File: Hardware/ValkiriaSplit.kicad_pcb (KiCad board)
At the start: 2 copper layers, 284.5 x 111.4 mm, 320 parts, among them J1 BAT, J2 TagConnect, J3 0.96_TFT_MODULE, J4 BAT, J5 TagConnect, J6 0.96_TFT_MODULE, Q1 AO3401A, Q2 AO3401A, Q3 AO3401A, Q4 AO3401A, SW1 MSK12C02, SW10 PG1350, SW11 PG1350, SW12 PG1350, SW13 PG1350, SW14 PG1350, SW15 PG1350, SW16 PG1350, SW17 PG1350, SW18 PG1350, SW19 PG1350, SW2 SW_Push, SW20 PG1350, SW21 PG1350, SW22 PG1350, SW23 PG1350, SW24 PG1350, SW25 PG1350, SW26 PG1350, SW27 PG1350, SW28 PG1350, SW29 PG1350, SW3 MSK12C02, SW30 PG1350, SW31 PG1350, SW32 PG1350, SW33 PG1350, SW34 PG1350, SW35 PG1350, SW36 PG1350, SW37 ENCODER, SW38 PG1350, SW39 PG1350, SW4 MSK12C02, SW40 PG1350, SW41 PG1350, SW42 PG1350, SW43 PG1350, SW44 PG1350, SW45 PG1350, SW46 PG1350, SW47 PG1350, SW48 PG1350, SW49 PG1350, SW5 SW_Push, SW50 PG1350, SW51 PG1350, SW52 PG1350, SW53 PG1350, SW54 PG1350, SW55 PG1350, SW56 PG1350, SW57 PG1350, SW58 PG1350, SW59 PG1350, SW6 MSK12C02, SW60 PG1350, SW61 PG1350, SW62 PG1350, SW63 PG1350, SW64 PG1350, SW65 PG1350, SW66 PG1350, SW67 PG1350, SW68 ENCODER, SW7 PG1350, SW8 PG1350, SW9 PG1350, U1 XIAO-NRF52840-PLUS, U2 TPS61040DBV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

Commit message: MIP display and LED enable
Return of the LED enable via GPIO.
Changed the TFT display for a MPI panel. It's more expensive than an e-ink one, but the sharpness is really nice.
Need to remove the numbers row to go for a true Corne-ish layout.
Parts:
- removed the C43 at (113.0, 215.9)
- removed the C44 at (113.0, 218.4)
- removed the C75 at (259.0, 216.8)
- removed the C76 at (259.0, 219.3)
- removed the D120 at (258.8, 226.8)
- removed the D5 at (208.5, 234.0)
- removed the D6 at (313.2, 229.1)
- removed the D60 at (112.7, 225.9)
- removed Q3, Q4: AO3401A, Package_TO_SOT_SMD:SOT-23
- removed R21: 10K, Resistor_SMD:R_0603_1608Metric
- removed R22: 22, Resistor_SMD:R_0603_1608Metric
- removed R23, R24, R25, R26: 0, Resistor_SMD:R_0603_1608Metric
- removed the SW5 at (330.8, 229.5)
- removed the SW6 at (332.3, 225.0)
- removed the U2 at (180.0, 237.0)
- removed the U4 at (213.5, 237.0)
- added C13: 1n, Capacitor_SMD:C_0603_1608Metric, F.Cu at (254.0, 203.2)
- added C14: 1u, Capacitor_SMD:C_0603_1608Metric, F.Cu at (254.0, 205.7)
- added C45: 100n, Capacitor_SMD:C_0603_1608Metric, F.Cu at (112.3, 211.4)
- added C46: 100n, Capacitor_SMD:C_0603_1608Metric, F.Cu at (112.3, 213.9)
- added C77: 100n, Capacitor_SMD:C_0603_1608Metric, F.Cu at (280.3, 209.3)
- added C78: 100n, Capacitor_SMD:C_0603_1608Metric, F.Cu at (280.3, 211.8)
- added D118: 1N4148WT, Diode_SMD:D_SOD-523, F.Cu at (284.1, 209.3)
- added D58: 1N4148WT, Diode_SMD:D_SOD-523, F.Cu at (116.1, 211.3)
- added FB1: 600, Inductor_SMD:L_0603_1608Metric, F.Cu at (125.8, 209.8)
- added FB2: 600, Inductor_SMD:L_0603_1608Metric, F.Cu at (129.8, 197.2)
- added FB3: 600, Inductor_SMD:L_0603_1608Metric, F.Cu at (254.0, 208.2)
- added FB4: 600, Inductor_SMD:L_0603_1608Metric, F.Cu at (258.0, 195.7)
- added U1: TPS61040DBV, Package_TO_SOT_SMD:SOT-23-5, F.Cu at (126.4, 230.2)
- added U3: TPS61040DBV, Package_TO_SOT_SMD:SOT-23-5, F.Cu at (254.6, 228.6)
- C10: value 4.7u -> 10p; footprint Capacitor_SMD:C_1206_3216Metric -> Capacitor_SMD:C_0603_1608Metric
- C11: value 1u -> 4.7u; footprint Capacitor_SMD:C_0603_1608Metric -> Capacitor_SMD:C_1206_3216Metric
- C6: value 1u -> 1n
- C8: value 4.7u -> 1u; footprint Capacitor_SMD:C_1206_3216Metric -> Capacitor_SMD:C_0603_1608Metric
- C9: value 10p -> 4.7u; footprint Capacitor_SMD:C_0603_1608Metric -> Capacitor_SMD:C_1206_3216Metric
- J3, J6: value 0.96_TFT_MODULE -> 1.08_MIP_MODULE; footprint Custom_Parts:0.96_TFT_MODULE -> Custom_Parts:1.08_MIP_MODULE
- R1: value 100K -> 500
- R10: value 10K -> 100K
- R11: value 22 -> 10K
- R12: value 100K -> 470K
- R13: value 500 -> 150K
- R14: value 470K -> 0
- R15: value 150K -> 0
- R19, R8: value 100 -> 0
- R2: value 500 -> 100K
- R20: value 10K -> 0
- R3: value 470K -> 10K
- R4: value 150K -> 470K
- R5: value 0 -> 150K
- R9: value 10K -> 500
- SW4: value MSK12C02 -> SW_Push; footprint Custom_Parts:MSK12C02 -> Button_Switch_SMD:SW_SPST_TS-1088-xR020
- moved SW3 187.6 mm to (257.1, 224.0)
- moved D3 179.7 mm to (266.8, 196.1)
- moved R17 176.3 mm to (112.3, 216.4)
- moved R18 176.3 mm to (112.3, 218.9)
- moved R10 175.2 mm to (258.0, 200.7)
- moved R11 175.2 mm to (258.0, 203.2)
- moved R9 175.2 mm to (258.0, 198.2)
- moved Q2 163.7 mm to (259.6, 228.4)
- moved C7 109.0 mm to (125.8, 207.3)
- moved C1 81.6 mm to (125.8, 197.2)
- moved R1 77.8 mm to (129.8, 199.7)
- moved SW2 76.7 mm to (139.4, 204.9)
- moved R14 68.9 mm to (262.1, 195.7)
- moved D1 66.0 mm to (138.6, 197.6)
- moved R15 65.2 mm to (262.1, 198.2)
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- renumbered C13 to C15, C14 to C16, C15 to C17, C16 to C18, C17 to C19, C18 to C20, C19 to C21, C20 to C22, C21 to C23, C22 to C24, C23 to C25, C24 to C26, C25 to C27, C26 to C28, C27 to C29, C28 to C30, C29 to C31, C30 to C32, C31 to C33, C32 to C34, C33 to C35, C34 to C36, C35 to C37, C36 to C38, C37 to C39, C38 to C40, C39 to C41, C40 to C42, C41 to C43, C42 to C44, C45 to C47, C46 to C48, C47 to C49, C48 to C50, C49 to C51, C50 to C52, C51 to C53, C52 to C54, C53 to C55, C54 to C56, C55 to C57, C56 to C58, C57 to C59, C58 to C60, C59 to C61, C60 to C62, C61 to C63, C62 to C64, C63 to C65, C64 to C66, C65 to C67, C66 to C68, C67 to C69, C68 to C70, C69 to C71, C70 to C72, C71 to C73, C72 to C74, C73 to C75, C74 to C76, D12 to D10, D102 to D100, D103 to D101, D104 to D102, D105 to D103, D106 to D104, D107 to D105, D108 to D106, D109 to D107, D110 to D108, D111 to D109, D13 to D11, D112 to D110, D113 to D111, D114 to D112, D115 to D113, D116 to D114, D117 to D115, D118 to D116, D119 to D117, D121 to D119, D14 to D12, D122 to D120, D123 to D121, D124 to D122, D125 to D123, D126 to D124, D15 to D13, D16 to D14, D17 to D15, D18 to D16, D19 to D17, D20 to D18, D21 to D19, D22 to D20, D23 to D21, D24 to D22, D25 to D23, D26 to D24, D27 to D25, D28 to D26, D29 to D27, D30 to D28, D31 to D29, D32 to D30, D33 to D31, D34 to D32, D35 to D33, D36 to D34, D37 to D35, D38 to D36, D39 to D37, D40 to D38, D41 to D39, D42 to D40, D43 to D41, D44 to D42, D45 to D43, D46 to D44, D47 to D45, D48 to D46, D49 to D47, D50 to D48, D51 to D49, D7 to D5, D52 to D50, D53 to D51, D54 to D52, D55 to D53, D56 to D54, D57 to D55, D58 to D56, D59 to D57, D61 to D59, D8 to D6, D62 to D60, D63 to D61, D64 to D62, D65 to D63, D66 to D64, D67 to D65, D68 to D66, D69 to D67, D70 to D68, D71 to D69, D9 to D7, D72 to D70, D73 to D71, D74 to D72, D75 to D73, D76 to D74, D77 to D75, D78 to D76, D79 to D77, D80 to D78, D81 to D79, D10 to D8, D82 to D80, D83 to D81, D84 to D82, D85 to D83, D86 to D84, D87 to D85, D88 to D86, D89 to D87, D90 to D88, D91 to D89, D11 to D9, D92 to D90, D93 to D91, D94 to D92, D95 to D93, D96 to D94, D97 to D95, D98 to D96, D99 to D97, D100 to D98, D101 to D99, SW12 to SW10, SW13 to SW11, SW14 to SW12, SW15 to SW13, SW16 to SW14, SW17 to SW15, SW18 to SW16, SW19 to SW17, SW20 to SW18, SW21 to SW19, SW22 to SW20, SW23 to SW21, SW24 to SW22, SW25 to SW23, SW26 to SW24, SW27 to SW25, SW28 to SW26, SW29 to SW27, SW30 to SW28, SW31 to SW29, SW32 to SW30, SW33 to SW31, SW34 to SW32, SW35 to SW33, SW36 to SW34, SW37 to SW35, SW38 to SW36, SW39 to SW37, SW40 to SW38, SW41 to SW39, SW42 to SW40, SW43 to SW41, SW44 to SW42, SW45 to SW43, SW46 to SW44, SW47 to SW45, SW48 to SW46, SW49 to SW47, SW50 to SW48, SW51 to SW49, SW7 to SW5, SW52 to SW50, SW53 to SW51, SW54 to SW52, SW55 to SW53, SW56 to SW54, SW57 to SW55, SW58 to SW56, SW59 to SW57, SW60 to SW58, SW61 to SW59, SW8 to SW6, SW62 to SW60, SW63 to SW61, SW64 to SW62, SW65 to SW63, SW66 to SW64, SW67 to SW65, SW68 to SW66, SW9 to SW7, SW10 to SW8, SW11 to SW9, U1 to U2, U3 to U4
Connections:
- C10 pad 2: GND -> /Control_Right/VFB
- C11 pad 1: /Control_Right/LCD_RES -> 5VR
- C12 pad 1: 3V3R -> /Control_Right/MIP_VDDA
- C12 pad 2: GND -> /Control_Right/MIP_VSSA
- C5 pad 1: /Control_Left/LCD_RES -> /Control_Left/MIP_VDDA
- C5 pad 2: GND -> /Control_Left/MIP_VSSA
- C6 pad 1: 3V3L -> /Control_Left/MIP_EN
- C7 pad 1: VBUSR -> 3V3L
- C8 pad 1: VREGR -> VBUSR
- C9 pad 1: 5VR -> VREGR
- C9 pad 2: /Control_Right/VFB -> GND
- D1 pad 1: /Control_Left/VCOM -> VREGL
- D3 pad 1: 3V3L -> VREGR
- D3 pad 2: /Control_Left/LCD_RES -> VBUSR
- D4 pad 1: /Control_Right/VCOM -> 5VR
- D4 pad 2: VBUSR -> /Control_Right/VSW
- J3 pad 1: /Control_Left/BKL -> /Control_Left/MIP_SCK
- J3 pad 2: GND -> /Control_Left/MIP_MOSI
- J3 pad 3: /Control_Left/LCD_RES -> /Control_Left/MIP_CS
- J3 pad 4: /Control_Left/LCD_DC -> GND
- J3 pad 5: /Control_Left/LCD_MOSI -> /Control_Left/MIP_EN
- J3 pad 6: /Control_Left/LCD_SCK -> /Control_Left/MIP_VDDA
- J3 pad 8: /Control_Left/LCD_CS -> GND
- J6 pad 1: /Control_Right/BKL -> /Control_Right/MIP_SCK
- J6 pad 2: GND -> /Control_Right/MIP_MOSI
- J6 pad 3: /Control_Right/LCD_RES -> /Control_Right/MIP_CS
- J6 pad 4: /Control_Right/LCD_DC -> GND
- J6 pad 5: /Control_Right/LCD_MOSI -> /Control_Right/MIP_EN
- J6 pad 6: /Control_Right/LCD_SCK -> /Control_Right/MIP_VDDA
- J6 pad 8: /Control_Right/LCD_CS -> GND
- Q1 pad 2: /Control_Left/VCOM -> VREGL
- Q2 pad 1: /Control_Left/BKLG -> VBUSR
- Q2 pad 2: /Control_Left/BKLD -> VREGR
- Q2 pad 3: 3V3L -> VBATR
- R1 pad 1: VBUSL -> /Control_Left/LED_DATA
- R1 pad 2: GND -> LED_DATA_L
- R10 pad 1: /Control_Left/BKLD -> VBUSR
- R10 pad 2: /Control_Left/BKLG -> GND
- R11 pad 1: /Control_Left/BKLD -> GND
- R11 pad 2: /Control_Left/BKL -> /Control_Right/LED_EN
- R12 pad 1: VBUSR -> 5VR
- R12 pad 2: GND -> /Control_Right/VFB
- R13 pad 1: /Control_Right/LED_DATA -> /Control_Right/VFB
- R13 pad 2: LED_DATA_R -> GND
- R14 pad 1: 5VR -> Net-(U4-P1.15_MOSI)
- R14 pad 2: /Control_Right/VFB -> /Control_Right/MIP_MOSI
- R15 pad 1: /Control_Right/VFB -> Net-(U4-P1.14_MISO)
- R15 pad 2: GND -> /Control_Right/MIP_CS
- R16 pad 1: Net-(U3-P1.15_MOSI) -> Net-(U4-P1.13_SCK)
- R16 pad 2: /Control_Right/LCD_MOSI -> /Control_Right/MIP_SCK
- R17 pad 1: Net-(U3-P1.14_MISO) -> ENC_CW_L
- R17 pad 2: /Control_Right/LCD_DC -> /Matrix_Left/ENC_CW
- R18 pad 1: Net-(U3-P1.13_SCK) -> ENC_CC_L
- R18 pad 2: /Control_Right/LCD_SCK -> /Matrix_Left/ENC_CC
- R19 pad 1: /Control_Right/LCD_BKL -> ENC_CW_R
- R19 pad 2: /Control_Right/BKLG -> /Matrix_Right/ENC_CW
- R2 pad 1: /Control_Left/LED_DATA -> VBUSL
- R2 pad 2: LED_DATA_L -> GND
- R20 pad 1: 3V3R -> ENC_CC_R
- R20 pad 2: /Control_Right/LCD_RES -> /Matrix_Right/ENC_CC
- R3 pad 1: 5VL -> GND
- R3 pad 2: /Control_Left/VFB -> /Control_Left/LED_EN
- R4 pad 1: /Control_Left/VFB -> 5VL
- R4 pad 2: GND -> /Control_Left/VFB
- R5 pad 1: Net-(U1-P1.15_MOSI) -> /Control_Left/VFB
- R5 pad 2: /Control_Left/LCD_MOSI -> GND
- R6 pad 1: Net-(U1-P1.14_MISO) -> Net-(U2-P1.15_MOSI)
- R6 pad 2: /Control_Left/LCD_DC -> /Control_Left/MIP_MOSI
- R7 pad 1: Net-(U1-P1.13_SCK) -> Net-(U2-P1.14_MISO)
- R7 pad 2: /Control_Left/LCD_SCK -> /Control_Left/MIP_CS
- R8 pad 1: /Control_Left/LCD_BKL -> Net-(U2-P1.13_SCK)
- R8 pad 2: /Control_Left/BKLG -> /Control_Left/MIP_SCK
- R9 pad 1: 3V3L -> /Control_Right/LED_DATA
- R9 pad 2: /Control_Left/LCD_RES -> LED_DATA_R
- SW3 pad 2: /Control_Left/VCOM -> /Control_Right/VBAT
- SW3 pad 3: VREGL -> VBATR
- SW4 pad 1: unconnected-(SW4-A-Pad1) -> /Control_Right/~{RESET}
- SW4 pad 2: /Control_Right/VBAT -> GND
- U2 pad 10: Net-(U1-P1.14_MISO) -> Net-(U2-P1.14_MISO)
- U2 pad 11: Net-(U1-P1.15_MOSI) -> Net-(U2-P1.15_MOSI)
- U2 pad 22: /Control_Left/LCD_BKL -> /Control_Left/MIP_EN
- U2 pad 7: /Control_Left/LCD_CS -> /Control_Left/LED_EN
- U2 pad 9: Net-(U1-P1.13_SCK) -> Net-(U2-P1.13_SCK)
- U4 pad 10: Net-(U3-P1.14_MISO) -> Net-(U4-P1.14_MISO)
- U4 pad 11: Net-(U3-P1.15_MOSI) -> Net-(U4-P1.15_MOSI)
- U4 pad 22: /Control_Right/LCD_BKL -> /Control_Right/MIP_EN
- U4 pad 7: /Control_Right/LCD_CS -> /Control_Right/LED_EN
- U4 pad 9: Net-(U3-P1.13_SCK) -> Net-(U4-P1.13_SCK)
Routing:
- removed copper zone on F.Cu, net /Control_Left/VFB
- removed copper zone on F.Cu, net /Control_Left/VSW
- removed copper zone on F.Cu, net /Control_Right/VFB
- removed copper zone on F.Cu, net /Control_Right/VSW
- removed copper zone on F.Cu, net VREGL
- removed copper zone on F.Cu, net VREGR

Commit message: Row removal and key layout
Removed the number row.
Adjusted the spacebar position and changed it to 1u.
Need to consider what to do for one of the halfs if its screen is to be removed.
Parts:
- removed the C16 at (160.6, 72.0)
- removed the C19 at (141.5, 69.6)
- removed the C23 at (122.5, 67.2)
- removed the C27 at (103.4, 69.6)
- removed the C31 at (84.4, 74.4)
- removed the C35 at (65.3, 74.4)
- removed the C48 at (242.9, 77.3)
- removed the C51 at (262.0, 75.0)
- removed the C55 at (281.0, 72.5)
- removed the C59 at (300.1, 75.0)
- removed the C63 at (319.1, 79.8)
- removed C67: 1u, Capacitor_SMD:C_0603_1608Metric
- removed D105, D114: 1N4148WT, Diode_SMD:D_SOD-523
- removed the D11 at (154.3, 79.9)
- removed D110: SK6812MINI-E, Custom_Parts:LED_SK6812MINI-E_3.2x2.8mm_P1.5mm_ReverseMount
- removed the D18 at (124.4, 70.2)
- removed the D20 at (135.2, 77.5)
- removed the D27 at (105.4, 72.6)
- removed the D29 at (116.2, 75.1)
- removed the D36 at (86.3, 77.4)
- removed the D38 at (97.1, 77.5)
- removed the D45 at (78.1, 82.3)
- removed the D50 at (67.3, 77.4)
- removed the D54 at (59.0, 82.3)
- removed the D6 at (162.5, 75.0)
- removed the D66 at (237.5, 75.0)
- removed the D69 at (256.5, 72.6)
- removed the D71 at (229.2, 79.9)
- removed the D78 at (275.6, 70.2)
- removed the D80 at (248.2, 77.5)
- removed the D87 at (294.6, 72.6)
- removed the D89 at (267.3, 75.1)
- removed the D9 at (143.5, 72.6)
- removed the D96 at (313.7, 77.4)
- removed the D98 at (286.3, 77.5)
- removed the SW10 at (140.9, 82.6)
- removed the SW15 at (121.9, 80.2)
- removed the SW20 at (102.8, 82.6)
- removed the SW25 at (83.8, 87.4)
- removed the SW30 at (64.8, 87.4)
- removed the SW36 at (234.9, 85.0)
- removed the SW41 at (254.0, 82.6)
- removed the SW46 at (273.0, 80.2)
- removed the SW5 at (160.0, 85.0)
- removed the SW51 at (292.1, 82.6)
- removed SW56, SW61: PG1350, Custom_Parts:PG1350_1.00u_PCB
- moved J6 103.4 mm to (216.5, 220.6)
- moved SW54 80.8 mm to (238.7, 211.7)
- moved D62 15.4 mm to (217.7, 168.1), turned to -66 degrees
- moved SW33 12.6 mm to (225.0, 170.4), turned to -156 degrees
- moved SW8 10.6 mm to (170.3, 168.4), turned to 156 degrees
- moved D14 8.99 mm to (167.1, 161.4), turned to -114 degrees
- moved J2 8.60 mm to (183.6, 85.0)
- moved J5 8.60 mm to (216.4, 85.0)
- moved C23 7.86 mm to (176.1, 156.7), turned to -24 degrees
- moved U2 6.00 mm to (183.6, 75.0)
- moved U4 6.00 mm to (216.4, 75.0)
- moved SW29 5.47 mm to (183.6, 139.5)
- moved D65 4.93 mm to (223.3, 160.3), turned to 24 degrees
- moved D17 4.93 mm to (176.7, 160.3), turned to 156 degrees
- moved C49 4.36 mm to (229.2, 160.2), turned to 24 degrees
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- renumbered C44 to C15, C41 to C16, C42 to C17, C40 to C18, C37 to C19, C38 to C20, C36 to C21, C33 to C22, C34 to C23, C32 to C24, C29 to C25, C30 to C26, C28 to C27, C25 to C28, C26 to C29, C24 to C30, C21 to C31, C22 to C32, C20 to C33, C17 to C34, C18 to C35, C43 to C36, C39 to C37, C15 to C38, C45 to C39, C46 to C40, C76 to C41, C73 to C42, C74 to C43, C72 to C44, C69 to C45, C70 to C46, C68 to C47, C65 to C48, C66 to C49, C64 to C50, C61 to C51, C62 to C52, C60 to C53, C57 to C54, C58 to C55, C53 to C57, C54 to C58, C52 to C59, C49 to C60, C50 to C61, C75 to C62, C71 to C63, C47 to C64, C77 to C65, C78 to C66, D53 to D10, D65 to D100, D12 to D11, D13 to D12, D14 to D13, D15 to D14, D51 to D15, D43 to D16, D44 to D17, D21 to D18, D22 to D19, D23 to D20, D24 to D21, D37 to D22, D34 to D23, D35 to D24, D30 to D25, D31 to D26, D32 to D27, D33 to D28, D28 to D29, D39 to D30, D40 to D31, D41 to D32, D42 to D33, D25 to D34, D26 to D35, D19 to D36, D46 to D37, D47 to D38, D48 to D39, D49 to D40, D16 to D41, D17 to D42, D10 to D43, D55 to D44, D56 to D45, D57 to D46, D58 to D47, D7 to D48, D8 to D49, D64 to D5, D63 to D50, D59 to D51, D5 to D52, D124 to D53, D121 to D54, D122 to D55, D120 to D56, D112 to D57, D113 to D58, D72 to D59, D61 to D6, D73 to D60, D74 to D61, D75 to D62, D111 to D63, D103 to D64, D104 to D65, D81 to D66, D82 to D67, D83 to D68, D84 to D69, D62 to D7, D97 to D70, D94 to D71, D95 to D72, D90 to D73, D91 to D74, D92 to D75, D93 to D76, D88 to D77, D99 to D78, D100 to D79, D60 to D8, D101 to D80, D102 to D81, D85 to D82, D86 to D83, D79 to D84, D106 to D85, D107 to D86, D108 to D87, D109 to D88, D76 to D89, D52 to D9, D77 to D90, D70 to D91, D115 to D92, D116 to D93, D117 to D94, D118 to D95, D67 to D96, D68 to D97, D123 to D98, D119 to D99, SW12 to SW10, SW13 to SW11, SW14 to SW12, SW16 to SW13, SW17 to SW14, SW18 to SW15, SW19 to SW16, SW21 to SW17, SW22 to SW18, SW23 to SW19, SW24 to SW20, SW26 to SW21, SW27 to SW22, SW28 to SW23, SW29 to SW24, SW31 to SW25, SW32 to SW26, SW33 to SW27, SW34 to SW28, SW35 to SW29, SW37 to SW30, SW38 to SW31, SW39 to SW32, SW40 to SW33, SW42 to SW34, SW43 to SW35, SW44 to SW36, SW45 to SW37, SW47 to SW38, SW48 to SW39, SW49 to SW40, SW50 to SW41, SW52 to SW42, SW53 to SW43, SW54 to SW44, SW55 to SW45, SW57 to SW46, SW58 to SW47, SW59 to SW48, SW60 to SW49, SW6 to SW5, SW62 to SW50, SW63 to SW51, SW64 to SW52, SW65 to SW53, SW66 to SW54, SW7 to SW6, SW8 to SW7, SW9 to SW8, SW11 to SW9
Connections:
- D11 pad 1: ROW2_L -> ROW1_L
- D12 pad 1: ROW3_L -> ROW2_L
- D13 pad 1: ROW4_L -> ROW3_L
- D14 pad 1: ROW5_L -> ROW4_L
- D18 pad 1: ROW2_L -> ROW1_L
- D19 pad 1: ROW3_L -> ROW2_L
- D20 pad 1: ROW4_L -> ROW3_L
- D21 pad 1: ROW5_L -> ROW4_L
- D25 pad 1: ROW2_L -> ROW1_L
- D26 pad 1: ROW3_L -> ROW2_L
- D27 pad 1: ROW4_L -> ROW3_L
- D28 pad 1: ROW5_L -> ROW4_L
- D30 pad 1: ROW2_L -> ROW1_L
- D31 pad 1: ROW3_L -> ROW2_L
- D32 pad 1: ROW4_L -> ROW3_L
- D33 pad 1: ROW5_L -> ROW4_L
- D37 pad 1: ROW2_L -> ROW1_L
- D38 pad 1: ROW3_L -> ROW2_L
- D39 pad 1: ROW4_L -> ROW3_L
- D40 pad 1: ROW5_L -> ROW4_L
- D43 pad 2: Net-(D10-DIN) (its old number) -> Net-(D43-DIN)
- D44 pad 1: ROW2_L -> ROW1_L
- D45 pad 1: ROW3_L -> ROW2_L
- D46 pad 1: ROW4_L -> ROW3_L
- D47 pad 1: ROW5_L -> ROW4_L
- D48 pad 4: Net-(D10-DIN) (its old number) -> Net-(D48-DOUT)
- D50 pad 4: Net-(D61-DIN) -> Net-(D43-DIN)
- D51 pad 2: Net-(D50-DOUT) -> Net-(D48-DOUT)
- D54 pad 2: Net-(D121-DIN) -> LED_DATA_R
- D59 pad 1: ROW2_R -> ROW1_R
- D6 pad 2: Net-(D61-DIN) -> LED_DATA_L
- D60 pad 1: ROW3_R -> ROW2_R
- D61 pad 1: ROW4_R -> ROW3_R
- D62 pad 1: ROW5_R -> ROW4_R
- D66 pad 1: ROW2_R -> ROW1_R
- D67 pad 1: ROW3_R -> ROW2_R
- D68 pad 1: ROW4_R -> ROW3_R
- D69 pad 1: ROW5_R -> ROW4_R
- D73 pad 1: ROW2_R -> ROW1_R
- D74 pad 1: ROW3_R -> ROW2_R
- D75 pad 1: ROW4_R -> ROW3_R
- D76 pad 1: ROW5_R -> ROW4_R
- D78 pad 1: ROW2_R -> ROW1_R
- D79 pad 1: ROW3_R -> ROW2_R
- D80 pad 1: ROW4_R -> ROW3_R
- D81 pad 1: ROW5_R -> ROW4_R
- D85 pad 1: ROW2_R -> ROW1_R
- D86 pad 1: ROW3_R -> ROW2_R
- D87 pad 1: ROW4_R -> ROW3_R
- D88 pad 1: ROW5_R -> ROW4_R
- D91 pad 2: Net-(D67-DOUT) -> Net-(D91-DIN)
- D92 pad 1: ROW2_R -> ROW1_R
- D93 pad 1: ROW3_R -> ROW2_R
- D94 pad 1: ROW4_R -> ROW3_R
- D95 pad 1: ROW5_R -> ROW4_R
- D96 pad 4: Net-(D67-DOUT) -> Net-(D96-DOUT)
- D98 pad 4: Net-(D121-DIN) -> Net-(D91-DIN)
- D99 pad 2: Net-(D110-DOUT) -> Net-(D96-DOUT)
- U2 pad 6: ROW5_L -> unconnected-(U2-P0.05_SCL-Pad6)
- U4 pad 6: ROW5_R -> unconnected-(U4-P0.05_SCL-Pad6)
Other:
- board size 284.5 x 111.4 mm -> 284.5 x 92.4 mm

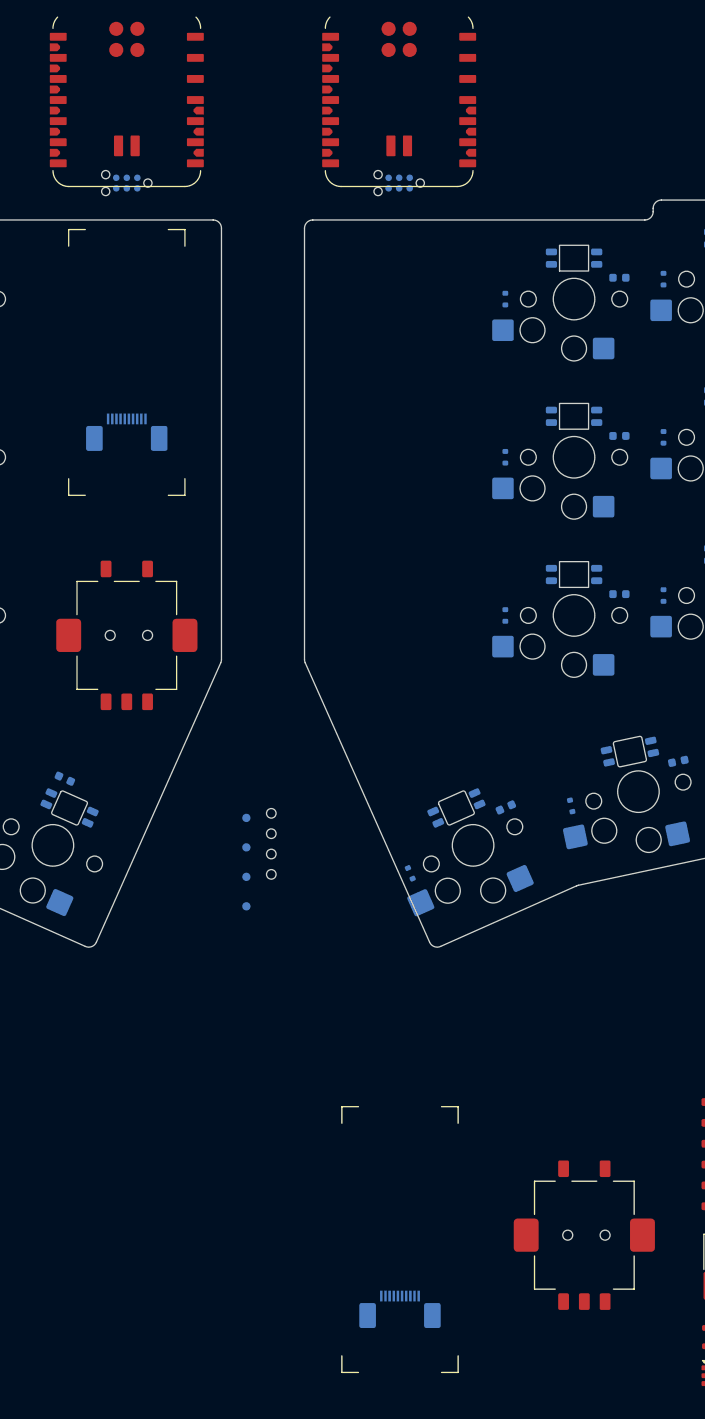
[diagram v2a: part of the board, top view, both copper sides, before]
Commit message: Debug connector
Updated the debug connector for a custom one.
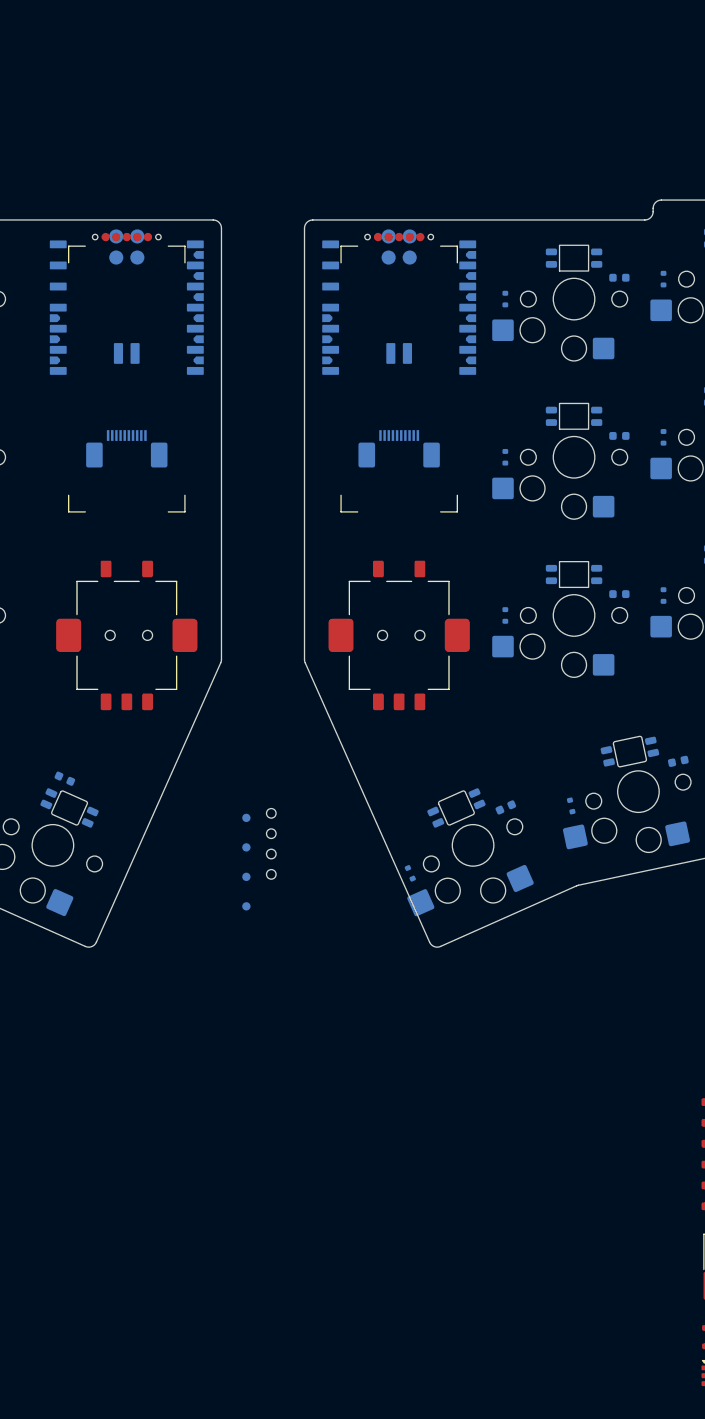
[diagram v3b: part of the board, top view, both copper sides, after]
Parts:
- C15, C16, C17, C18, C19, C20, C21, C22, C23, C24, C25, C26, C27, C28, C29, C30, C31, C32, C33, C34, C35, C36, C37, C38, C41, C42, C43, C44, C45, C46, C47, C48, C49, C50, C51, C52, C53, C54, C55, C56, C57, C58, C59, C60, C61, C62, C63, C64: value 1u -> 100n
- J2, J5: value TagConnect -> JTAG; footprint Connector:Tag-Connect_TC2030-IDC-NL_2x03_P1.27mm_Vertical -> Custom_Parts:JTAG_SWD_1X05_1.27MM_COMBO; moved to F.Cu
- U2, U4: moved to B.Cu
- moved J6 103.6 mm to (216.4, 117.0)
- moved SW54 75.6 mm to (216.4, 139.5)
- moved U2 25.0 mm to (183.6, 100.0)
- moved U4 25.0 mm to (216.4, 100.0)
- moved J2 7.53 mm to (179.8, 91.5), turned to 0 degrees
- moved J5 7.53 mm to (220.2, 91.5)
- moved J3 2.00 mm to (183.6, 117.0)

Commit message: Board outline and routing
Enlarged the board outline by 0.5mm for proper fitment of the switch receptacles.
Updated the footprint for the switch receptacles.
Changed the JTAG connector for a custom one.
Need to review the size of the PCB area dedicated to the MCU and the screen.
Need to consider removing the additional reset button.
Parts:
- C1, C10, C11, C12, C13, C14, C2, C3, C39, C4, C40, C5, C6, C65, C66, C7, C8, C9, D47, D95, FB1, FB2, FB3, FB4, J1, J4, L1, L2, Q1, Q2, R1, R10, R11, R12, R13, R14, R15, R16, R17, R18, R19, R2, R20, R3, R4, R5, R6, R7, R8, R9, SW1, SW2, SW3, SW4, U1, U3: moved to B.Cu
- D1, D2, D3, D4: value DSK24 -> DSL14; moved to B.Cu
- H1, H2, H3, H4: value MountingHole -> Tooling
- SW10, SW11, SW12, SW13, SW14, SW15, SW16, SW17, SW18, SW19, SW20, SW21, SW22, SW23, SW24, SW25, SW26, SW27, SW28, SW30, SW31, SW32, SW33, SW34, SW35, SW36, SW37, SW38, SW39, SW40, SW41, SW42, SW43, SW44, SW45, SW46, SW47, SW48, SW49, SW5, SW50, SW51, SW52, SW53, SW6, SW7, SW8, SW9: footprint Custom_Parts:PG1350_1.00u_PCB -> Custom_Parts:PG1350_1.00u_PCB_TIGHT
- moved SW4 130.4 mm to (216.4, 83.4), turned to 180 degrees
- moved SW2 129.3 mm to (183.6, 83.4), turned to 180 degrees
- moved R1 115.0 mm to (171.0, 92.4), turned to 180 degrees
- moved FB1 113.8 mm to (184.8, 112.4), turned to 90 degrees
- moved SW1 113.6 mm to (193.4, 132.0), turned to -90 degrees
- moved C7 112.8 mm to (186.8, 112.4), turned to 90 degrees
- moved R9 109.7 mm to (229.0, 92.4)
- moved C5 106.4 mm to (182.8, 112.4), turned to -90 degrees
- moved SW3 104.9 mm to (206.6, 132.0), turned to 90 degrees
- moved FB3 102.7 mm to (217.2, 112.4), turned to 90 degrees
- moved C14 99.6 mm to (219.2, 112.4), turned to 90 degrees
- moved FB2 99.0 mm to (180.8, 112.4), turned to -90 degrees
- moved C6 98.7 mm to (180.8, 122.8), turned to -90 degrees
- moved C12 96.5 mm to (215.2, 112.4), turned to -90 degrees
- moved R8 95.5 mm to (186.8, 122.8), turned to 90 degrees
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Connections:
- J2 pad 2: /Control_Left/SWDIO -> /Control_Left/SWDCLK
- J2 pad 3: /Control_Left/~{RESET} -> /Control_Left/SWDIO
- J2 pad 4: /Control_Left/SWDCLK -> /Control_Left/~{RESET}
- J5 pad 2: /Control_Right/SWDIO -> /Control_Right/SWDCLK
- J5 pad 3: /Control_Right/~{RESET} -> /Control_Right/SWDIO
- J5 pad 4: /Control_Right/SWDCLK -> /Control_Right/~{RESET}
- SW1 pad 1: unconnected-(SW1-A-Pad1) -> VBATL
- SW1 pad 3: VBATL -> unconnected-(SW1-C-Pad3)
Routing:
- net /Control_Left/MIP_VDDA: track 0.00 -> 9.06 mm, vias 0 -> 2
- net /Control_Right/MIP_VDDA: track 0.00 -> 9.06 mm, vias 0 -> 2
- net /Control_Right/MIP_EN: track 0.00 -> 7.97 mm
- net /Control_Left/MIP_EN: track 0.00 -> 7.97 mm
- net /Control_Right/MIP_CS: track 0.00 -> 7.51 mm
- net /Control_Left/MIP_CS: track 0.00 -> 7.51 mm
- net /Control_Right/MIP_SCK: track 0.00 -> 6.89 mm
- net /Control_Right/MIP_MOSI: track 0.00 -> 6.89 mm
- net /Control_Left/MIP_SCK: track 0.00 -> 6.89 mm
- net /Control_Left/MIP_MOSI: track 0.00 -> 6.89 mm
- net 3V3L: track 0.00 -> 5.23 mm
- net 3V3R: track 0.00 -> 5.23 mm
- net /Control_Right/MIP_VSSA: track 0.00 -> 4.53 mm
- net /Control_Left/MIP_VSSA: track 0.00 -> 4.53 mm
- net /Control_Right/SWDCLK: track 0.00 -> 4.16 mm, vias 0 -> 1
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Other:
- board size 284.5 x 92.4 mm -> 285.5 x 93.5 mm

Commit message: Layout and routing
Updated the position of some RGB LEDs.
Routed the left side columns.
This is a temporary commit in order to test different LED routing.
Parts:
- moved D10 95.3 mm to (67.3, 134.5)
- moved D22 95.3 mm to (162.5, 132.1)
- moved D29 95.3 mm to (162.5, 113.1)
- moved D34 78.0 mm to (86.3, 96.4)
- moved D41 77.5 mm to (67.3, 96.4)
- moved D48 57.6 mm to (67.3, 115.5)
- moved D15 57.4 mm to (143.5, 129.7)
- moved D36 57.4 mm to (143.5, 110.7)
- moved D7 57.4 mm to (86.3, 134.5)
- moved J4 41.0 mm to (240.0, 200.0)
- moved J1 40.9 mm to (160.0, 200.0)
- moved Q1 36.2 mm to (180.6, 208.7)
- moved C1 36.2 mm to (169.9, 196.4)
- moved R3 36.2 mm to (169.9, 204.0)
- moved U1 36.2 mm to (180.7, 204.3)
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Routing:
- net COL1_L: track 0.00 -> 76.0 mm
- net COL3_L: track 0.00 -> 72.7 mm
- net COL2_L: track 0.00 -> 72.4 mm
- net COL6_L: track 0.00 -> 65.3 mm
- net COL5_L: track 0.00 -> 65.3 mm
- net COL4_L: track 0.00 -> 65.3 mm
- net 5VL: track 0.00 -> 49.3 mm
- net Net-(U2-P1.15_MOSI): track 0.00 -> 40.7 mm
- net Net-(U2-P1.14_MISO): track 0.00 -> 32.9 mm
- net Net-(U2-P1.13_SCK): track 0.00 -> 30.3 mm, vias 0 -> 2
- net VBATL: track 0.00 -> 27.4 mm
- net /Control_Left/MIP_EN: track 7.97 -> 34.7 mm
- net VBUSL: track 0.00 -> 23.5 mm
- net /Control_Left/LED_DATA: track 0.00 -> 23.0 mm
- net 3V3L: track 5.23 -> 26.0 mm
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- added copper zone on B.Cu, net GND
- added copper zone on F.Cu, net GND
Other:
- outline, holes or cut-outs redrawn

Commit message: Display model and layout
Updated the 3D model and footprint for the MIP display. It now sits further from the PCB.
Continued the layout and routing of the left side PCB.
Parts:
- C11, C2, C4, C9: value 4.7u -> 10u; footprint Capacitor_SMD:C_1206_3216Metric -> Capacitor_SMD:C_0603_1608Metric
- J3, J6: footprint Custom_Parts:1.08_MIP_MODULE -> Custom_Parts:1.08_MIP_MODULE_TALL
- moved D23 99.0 mm to (176.7, 160.3), turned to 156 degrees
- moved D17 94.0 mm to (86.3, 134.5), turned to 180 degrees
- moved D34 89.9 mm to (155.8, 153.5), turned to 168 degrees
- moved D41 83.2 mm to (143.5, 129.7)
- moved D48 76.4 mm to (143.5, 110.7)
- moved D24 69.5 mm to (86.3, 153.6), turned to 180 degrees
- moved D35 66.7 mm to (67.3, 153.6)
- moved D51 61.9 mm to (143.5, 91.6)
- moved D22 59.5 mm to (105.4, 148.8)
- moved D16 57.4 mm to (162.5, 132.1)
- moved D52 57.2 mm to (67.3, 96.4)
- moved D29 47.6 mm to (134.0, 151.2)
- moved D49 42.6 mm to (67.3, 115.5)
- moved D42 40.7 mm to (67.3, 134.5)
- moved D15 38.1 mm to (105.4, 129.7)
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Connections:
- U2 pad 20: COL6_L -> unconnected-(U2-P0.31_BAT-Pad20)
- U2 pad 6: unconnected-(U2-P0.05_SCL-Pad6) -> COL6_L
- U4 pad 20: COL6_R -> unconnected-(U4-P0.31_BAT-Pad20)
- U4 pad 6: unconnected-(U4-P0.05_SCL-Pad6) -> COL6_R
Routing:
- net 5VL: track 49.3 -> 459.7 mm, vias 0 -> 24
- net ROW3_L: track 0.00 -> 152.6 mm, vias 0 -> 6
- net ROW2_L: track 0.00 -> 152.6 mm, vias 0 -> 6
- net ROW1_L: track 0.00 -> 152.6 mm, vias 0 -> 6
- net ROW4_L: track 0.00 -> 53.5 mm
- net COL1_L: track 76.0 -> 42.1 mm
- net Net-(D5-DIN): track 0.00 -> 32.1 mm
- net Net-(D15-DOUT): track 0.00 -> 32.1 mm
- net Net-(D15-DIN): track 0.00 -> 32.1 mm
- net Net-(D48-DOUT): track 0.00 -> 32.1 mm
- net Net-(D49-DOUT): track 0.00 -> 32.1 mm
- net Net-(D42-DOUT): track 0.00 -> 32.1 mm
- net Net-(D35-DOUT): track 0.00 -> 32.1 mm
- net Net-(D29-DIN): track 0.00 -> 32.0 mm
- net Net-(U2-P1.13_SCK): track 30.3 -> 0.00 mm, vias 2 -> 0
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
